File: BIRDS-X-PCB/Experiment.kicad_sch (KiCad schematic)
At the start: 19 parts, among them U1 LM334M, U2 ADG734, U301 VT01, U304 VT01, U305 VT01, U306 VT01, U307 LM335DT

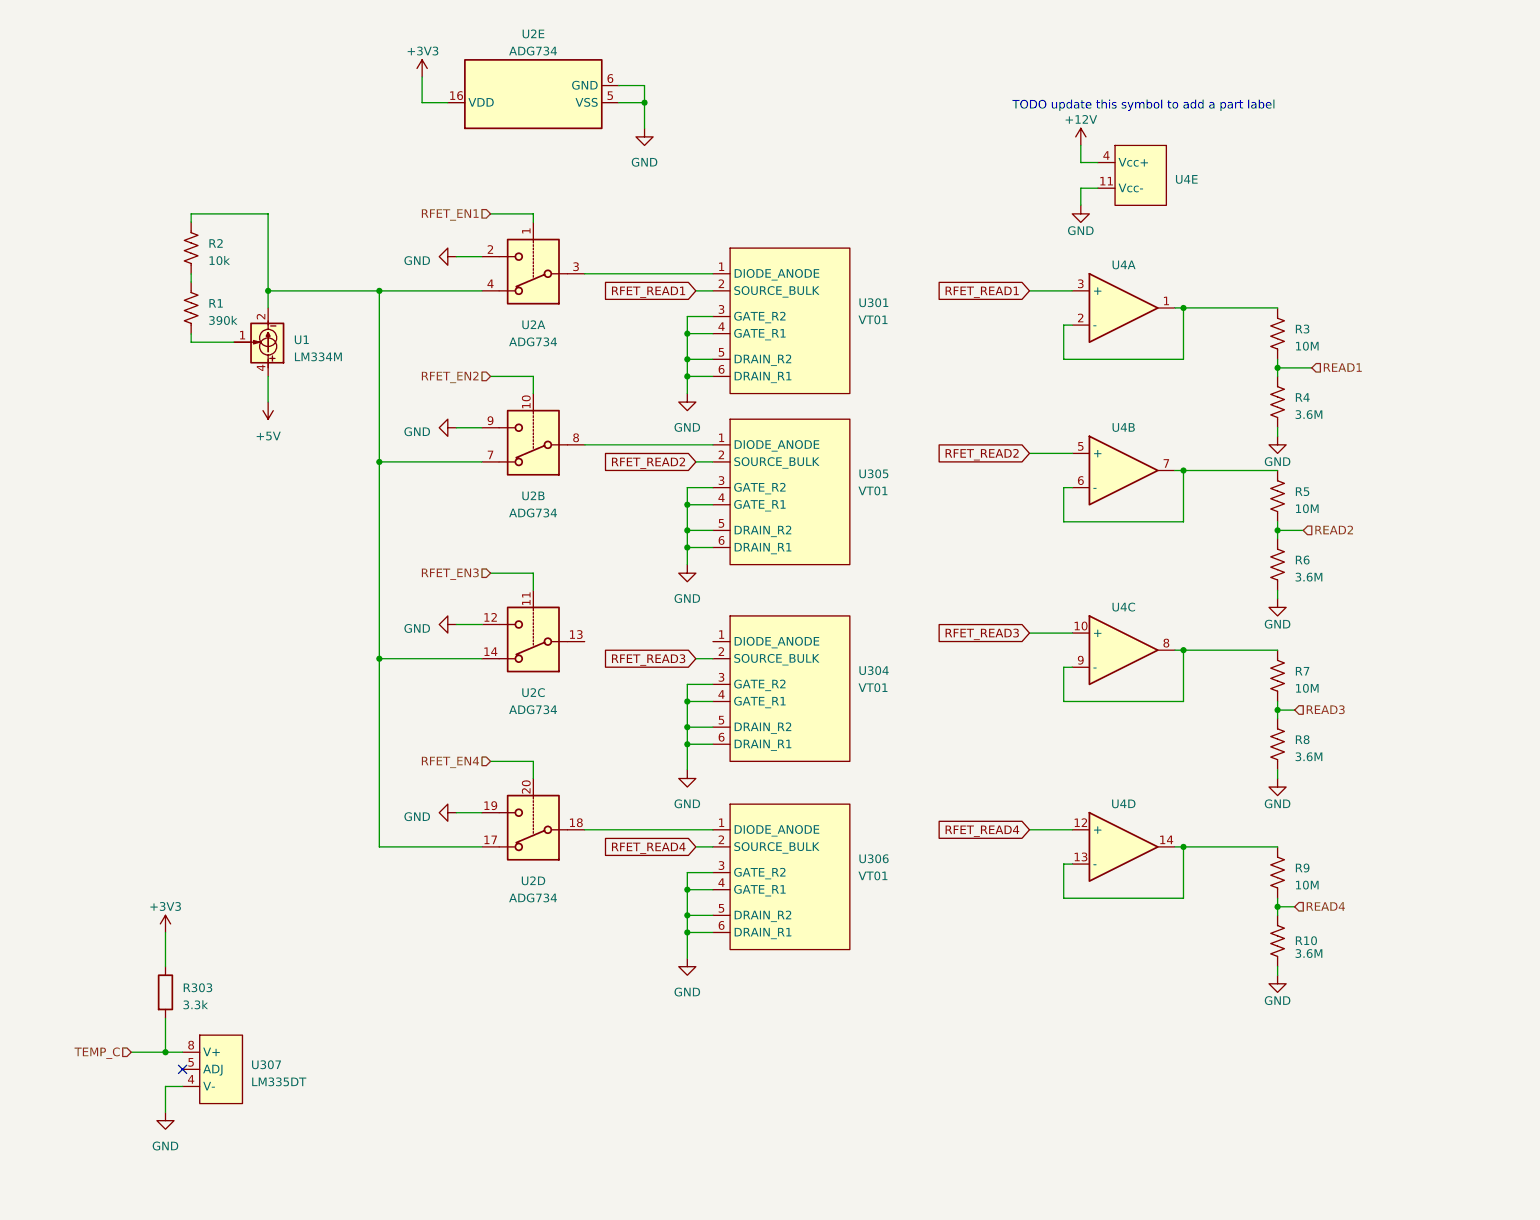
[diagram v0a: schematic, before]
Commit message: Semantic and symbol updates, begin review changes
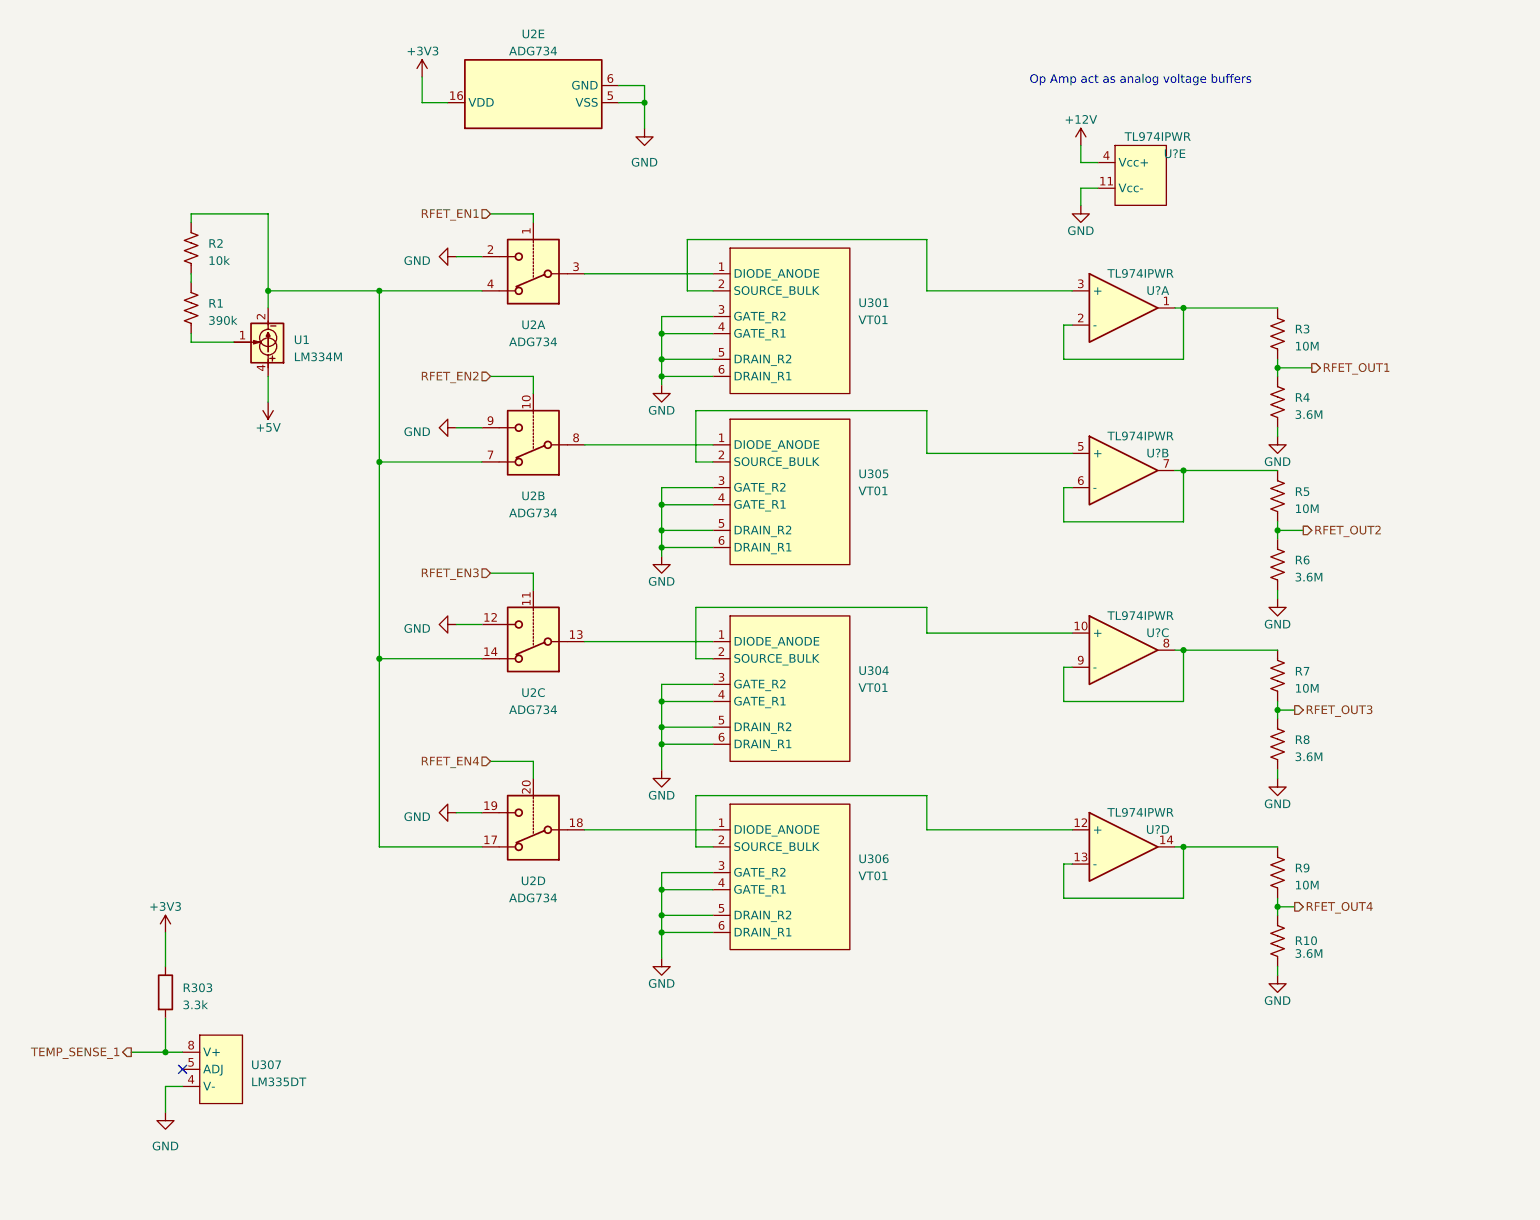
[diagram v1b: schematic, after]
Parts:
- U? (x5): renamed from U4; value ~ -> TL974IPWR
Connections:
- net at U2.13: now also U304.1 (DIODE_ANODE)
- net READ1 renamed RFET_OUT1
- net READ2 renamed RFET_OUT2
- net READ3 renamed RFET_OUT3
- net READ4 renamed RFET_OUT4
- net RFET_READ1: no longer names the net of U301.2 (SOURCE_BULK), U?.3 (+)
- net RFET_READ2: no longer names the net of U305.2 (SOURCE_BULK), U?.5 (+)
- net RFET_READ3: no longer names the net of U304.2 (SOURCE_BULK), U?.10 (+)
- net RFET_READ4: no longer names the net of U306.2 (SOURCE_BULK), U?.12 (+)
- net TEMP_C renamed TEMP_SENSE_1
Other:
- note added: "Op Amp act as analog voltage buffers"
- note removed: "TODO update this symbol to add a part label"

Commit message: Add more MCU changes
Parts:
- U302: renamed from U305; footprint (none) -> lib:SOP65P640X120-14N
- U305: renamed from U?; footprint lib:SOP65P640X120-14N -> (none)
- U306: renamed from U2; footprint Package_SO:TSSOP-20_4.4x6.5mm_P0.65mm -> (none)
- renumbered U304 to U303, U306 to U304, U1 to U308

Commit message: Implement oscillator improvements
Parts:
- U302: footprint lib:SOP65P640X120-14N -> (none)
- U307, U308: footprint Package_SO:SOIC-8_3.9x4.9mm_P1.27mm -> (none)
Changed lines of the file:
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@@
       (effects (font (size 1.27 1.27)) (justify left))
     )
-    (property "Footprint" "lib:SOP65P640X120-14N" (at 137.16 85.09 0)
+    (property "Footprint" "" (at 137.16 85.09 0)
       (effects (font (size 1.27 1.27)) hide)
     )
@@
       (effects (font (size 1.27 1.27)) (justify right))
     )
-    (property "Footprint" "Package_SO:SOIC-8_3.9x4.9mm_P1.27mm" (at 59.055 63.5 0)
+    (property "Footprint" "" (at 59.055 63.5 0)
       (effects (font (size 1.27 1.27) italic) (justify left) hide)
     )
@@
       (effects (font (size 1.27 1.27)) (justify left))
     )
-    (property "Footprint" "Package_SO:SOIC-8_3.9x4.9mm_P1.27mm" (at 55.88 181.61 0)
-      (effects (font (size 1.27 1.27)) hide)
-    )
+    (property "Footprint" "" (at 55.88 181.61 0)
+      (effects (font (size 1.27 1.27)) hide)
+    )

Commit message: Add logic level converters, etc.
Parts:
- U307: footprint (none) -> Package_SO:SOIC-8_3.9x4.9mm_P1.27mm; symbol BIRDS-X_Symbols_Lib:LM335DT -> BIRDS-X_Symbols_Lib:LM335D
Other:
- moved on the sheet: U307
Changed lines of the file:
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@@
   (junction (at 118.11 91.44) (diameter 0) (color 0 0 0 0)
   )
-  (no_connect (at 46.99 175.26))
+  (no_connect (at 41.91 181.61))
   (wire (pts (xy 195.58 113.03) (xy 194.31 113.03))
     (stroke (width 0) (type default))
@@
     (stroke (width 0) (type default))
   )
-  (wire (pts (xy 46.99 177.8) (xy 44.45 177.8))
-    (stroke (width 0) (type default))
-  )
   (wire (pts (xy 209.55 160.02) (xy 209.55 161.29))
     (stroke (width 0) (type default))
@@
     (stroke (width 0) (type default))
   )
-  (wire (pts (xy 44.45 177.8) (xy 44.45 181.61))
-    (stroke (width 0) (type default))
-  )
   (wire (pts (xy 118.11 127) (xy 125.73 127))
     (stroke (width 0) (type default))
   )
-  (wire (pts (xy 44.45 154.94) (xy 44.45 160.02))
+  (wire (pts (xy 44.45 157.48) (xy 44.45 160.02))
     (stroke (width 0) (type default))
   )
@@
     (stroke (width 0) (type default))
   )
+  (wire (pts (xy 46.99 189.23) (xy 46.99 190.5))
+    (stroke (width 0) (type default))
+  )
   (wire (pts (xy 209.55 95.25) (xy 209.55 96.52))
     (stroke (width 0) (type default))
@@
   )
   (wire (pts (xy 118.11 120.65) (xy 118.11 124.46))
+    (stroke (width 0) (type default))
+  )
+  (wire (pts (xy 46.99 172.72) (xy 46.99 173.99))
     (stroke (width 0) (type default))
   )
@@
     )
   )
-  (symbol (lib_id "power:+3V3") (at 44.45 154.94 0) (unit 1)
-    (in_bom yes) (on_board yes) (dnp no) (fields_autoplaced)
-    (property "Reference" "#PWR0207" (at 44.45 158.75 0)
-      (effects (font (size 1.27 1.27)) hide)
-    )
-    (property "Value" "+3V3" (at 44.45 151.13 0)
-      (effects (font (size 1.27 1.27)))
-    )
-    (property "Footprint" "" (at 44.45 154.94 0)
-      (effects (font (size 1.27 1.27)) hide)
-    )
-    (property "Datasheet" "" (at 44.45 154.94 0)
+  (symbol (lib_id "power:+3V3") (at 44.45 157.48 0) (unit 1)
+    (in_bom yes) (on_board yes) (dnp no) (fields_autoplaced)
+    (property "Reference" "#PWR0207" (at 44.45 161.29 0)
+      (effects (font (size 1.27 1.27)) hide)
+    )
+    (property "Value" "+3V3" (at 44.45 153.67 0)
+      (effects (font (size 1.27 1.27)))
+    )
+    (property "Footprint" "" (at 44.45 157.48 0)
+      (effects (font (size 1.27 1.27)) hide)
+    )
+    (property "Datasheet" "" (at 44.45 157.48 0)
       (effects (font (size 1.27 1.27)) hide)
     )
@@
     )
   )
-  (symbol (lib_id "power:GND") (at 44.45 181.61 0) (unit 1)
-    (in_bom yes) (on_board yes) (dnp no) (fields_autoplaced)
-    (property "Reference" "#PWR0306" (at 44.45 187.96 0)
-      (effects (font (size 1.27 1.27)) hide)
-    )
-    (property "Value" "GND" (at 44.45 186.69 0)
-      (effects (font (size 1.27 1.27)))
-    )
-    (property "Footprint" "" (at 44.45 181.61 0)
-      (effects (font (size 1.27 1.27)) hide)
-    )
-    (property "Datasheet" "" (at 44.45 181.61 0)
+  (symbol (lib_id "power:GND") (at 46.99 190.5 0) (unit 1)
+    (in_bom yes) (on_board yes) (dnp no)
+    (property "Reference" "#PWR0306" (at 46.99 196.85 0)
+      (effects (font (size 1.27 1.27)) hide)
+    )
+    (property "Value" "GND" (at 46.99 194.31 0)
+      (effects (font (size 1.27 1.27)))
+    )
+    (property "Footprint" "" (at 46.99 190.5 0)
+      (effects (font (size 1.27 1.27)) hide)
+    )
+    (property "Datasheet" "" (at 46.99 190.5 0)
       (effects (font (size 1.27 1.27)) hide)
     )
@@
     )
   )
-  (symbol (lib_id "BIRDS-X_Symbols_Lib:LM335DT") (at 55.88 176.53 0) (unit 1)
-    (in_bom yes) (on_board yes) (dnp no) (fields_autoplaced)
-    (property "Reference" "U307" (at 57.15 174.625 0)
-      (effects (font (size 1.27 1.27)) (justify left))
-    )
-    (property "Value" "LM335DT" (at 57.15 177.165 0)
-      (effects (font (size 1.27 1.27)) (justify left))
-    )
-    (property "Footprint" "" (at 55.88 181.61 0)
-      (effects (font (size 1.27 1.27)) hide)
-    )
-    (property "Datasheet" "https://www.mouser.ca/datasheet/2/389/lm135-1849523.pdf" (at 55.88 184.15 0)
-      (effects (font (size 1.27 1.27)) hide)
-    )
+  (symbol (lib_id "BIRDS-X_Symbols_Lib:LM335D") (at 46.99 181.61 0) (unit 1)
+    (in_bom yes) (on_board yes) (dnp no)
+    (property "Reference" "U307" (at 49.53 179.07 0)
+      (effects (font (size 1.27 1.27)) (justify left))
+    )
+    (property "Value" "LM335DT" (at 49.53 181.61 0)
+      (effects (font (size 1.27 1.27)) (justify left))
+    )
+    (property "Footprint" "Package_SO:SOIC-8_3.9x4.9mm_P1.27mm" (at 50.8 194.31 0)
+      (effects (font (size 1.27 1.27)) hide)
+    )
+    (property "Datasheet" "https://www.mouser.ca/datasheet/2/389/lm135-1849523.pdf" (at 50.8 196.85 0)
+      (effects (font (size 1.27 1.27)) hide)
+    )
+    (pin "1")
+    (pin "2")
+    (pin "3")
     (pin "4")
     (pin "5")
+    (pin "6")
+    (pin "7")
     (pin "8")
     (instances

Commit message: Add footprints
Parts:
- U305: footprint (none) -> Package_SO:TSSOP-14_4.4x5mm_P0.65mm
- U306: footprint (none) -> Package_SO:TSSOP-20_4.4x6.5mm_P0.65mm
- U308: footprint (none) -> Package_SO:SOIC-8_3.9x4.9mm_P1.27mm
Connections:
- net at U308.1: now also R2.1; no longer R1.2
- net at U306.14, U306.17, U306.4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: now also R1.2; no longer R2.1
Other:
- note added: "TODO confirm 5V is right here Parker thinks maybe it should be 12V or 24V"
- note added: "VT01 RADFETs Sense Radiation"
- moved on the sheet: R1, R2, U308
